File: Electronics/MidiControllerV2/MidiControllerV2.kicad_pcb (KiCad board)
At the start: 2 copper layers, 40 parts, among them J1 USB_B_Micro, J2 BOOT0_H, J3 BOOT1_H, J4 Conn_01x04_Male, J5 Conn_01x08_Male, J6 Conn_01x04_Male, SW1 Encoder, SW2 Encoder, SW3 SW_DPST, U1 AMS1117-3.3, U2 STM32F100C8Tx, Y1 Crystal

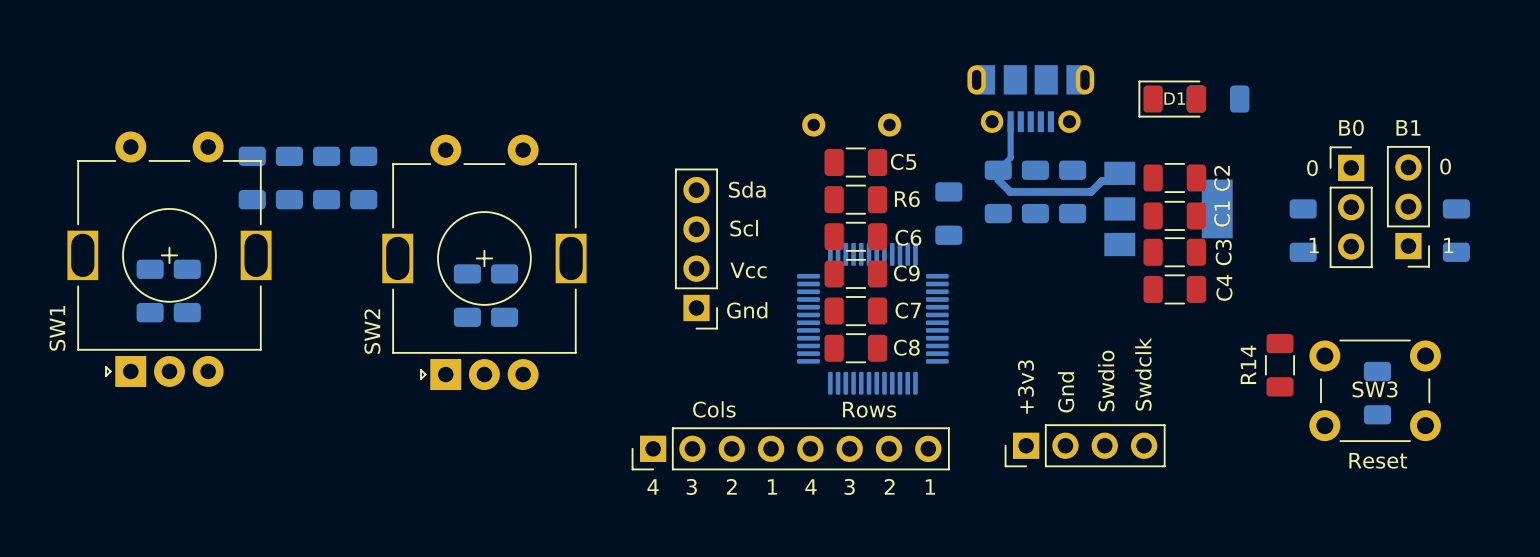
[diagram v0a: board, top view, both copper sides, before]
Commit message: #32 Pcb layout revised
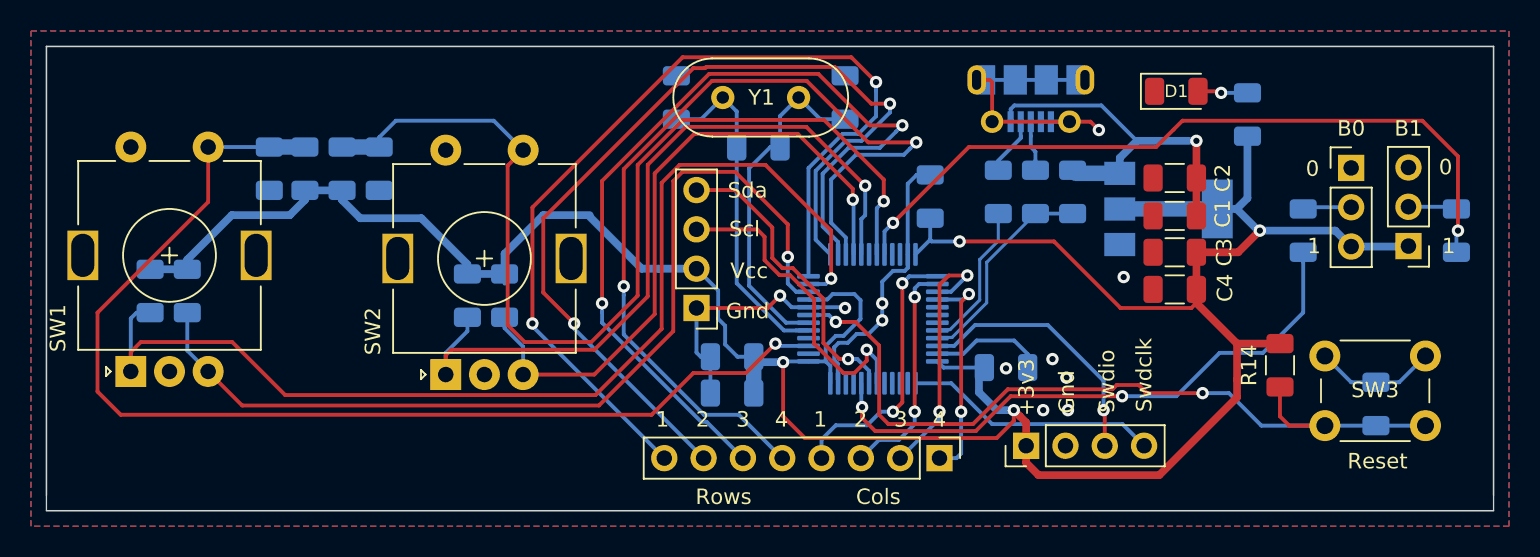
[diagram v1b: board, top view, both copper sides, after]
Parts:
- C5, C6, C7, C8, C9, R6: moved to B.Cu
- Y1: moved to F.Cu
- moved J5 18.5 mm to (131.2, 50.1), turned to 270 degrees
- moved C5 12.3 mm to (114.2, 26.8), turned to 90 degrees
- moved C9 11.1 mm to (117.8, 45.9), turned to 180 degrees
- moved Y1 10.9 mm to (117.2, 26.8), turned to 0 degrees
- moved C7 10.4 mm to (135.5, 44.2), turned to 0 degrees
- moved C6 9.03 mm to (125.1, 26.8), turned to 90 degrees
- moved C8 8.02 mm to (117.8, 43.5), turned to 180 degrees
- moved R6 7.16 mm to (119.5, 30.0), turned to 180 degrees
- moved R3 4.80 mm to (135.0, 32.9)
- moved R4 4.80 mm to (139.8, 32.9)
- moved R7 2.15 mm to (151.1, 27.9), turned to 90 degrees
- moved C10 1.63 mm to (130.6, 33.2)
- moved C12 1.25 mm to (87.9, 31.4)
- moved C13 1.17 mm to (95.0, 31.4)
- moved R12 1.17 mm to (90.2, 31.4)
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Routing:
- net +3V3: track 0.00 -> 185.0 mm, vias 0 -> 4
- net ENC1_SW: track 0.00 -> 73.5 mm, vias 0 -> 1
- net ENC1A: track 0.00 -> 71.2 mm, vias 0 -> 1
- net GND: track 0.00 -> 68.7 mm, vias 0 -> 11
- net ENC2_SW: track 0.00 -> 67.5 mm, vias 0 -> 1
- net KP_R1: track 0.00 -> 61.6 mm, vias 0 -> 2
- net ENC1B: track 0.00 -> 61.1 mm, vias 0 -> 1
- net KP_R2: track 0.00 -> 59.9 mm, vias 0 -> 2
- net KP_R4: track 0.00 -> 58.9 mm, vias 0 -> 2
- net KP_R3: track 0.00 -> 57.6 mm, vias 0 -> 2
- net RESET: track 0.00 -> 52.7 mm, vias 0 -> 2
- net ENC2A: track 0.00 -> 49.8 mm, vias 0 -> 1
- net BOOT1: track 0.00 -> 48.5 mm, vias 0 -> 2
- net ENC2B: track 0.00 -> 43.0 mm, vias 0 -> 1
- net BOOT0: track 0.00 -> 38.2 mm, vias 0 -> 2
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- added copper zone on B.Cu, net GND
- added copper zone on F.Cu, net GND
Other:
- board outline added: 93.5 x 30 mm

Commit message: #32 Updated pcb v1
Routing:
- net GND: track 68.7 -> 73.2 mm, vias 11 -> 13
- net +3V3: track 185.0 -> 184.4 mm
